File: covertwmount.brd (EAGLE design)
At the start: 50.8 x 33.5 mm, 56 parts, among them J1 B2B-PH-K-S(LF)(SN), U1 STM32G081RBT6, U2 MMBT4401-7-F

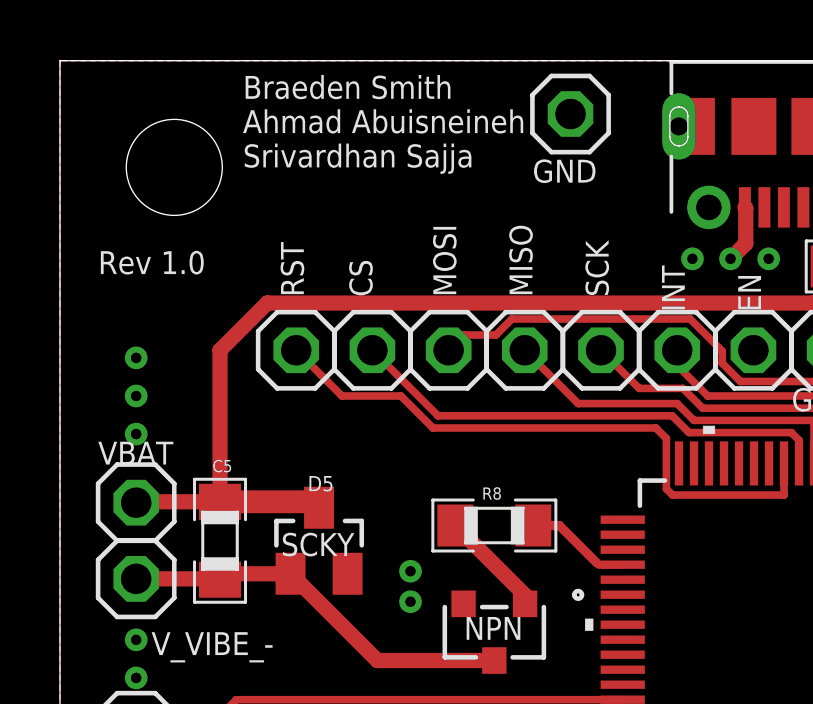
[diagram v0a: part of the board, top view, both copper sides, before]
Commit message: pairing button
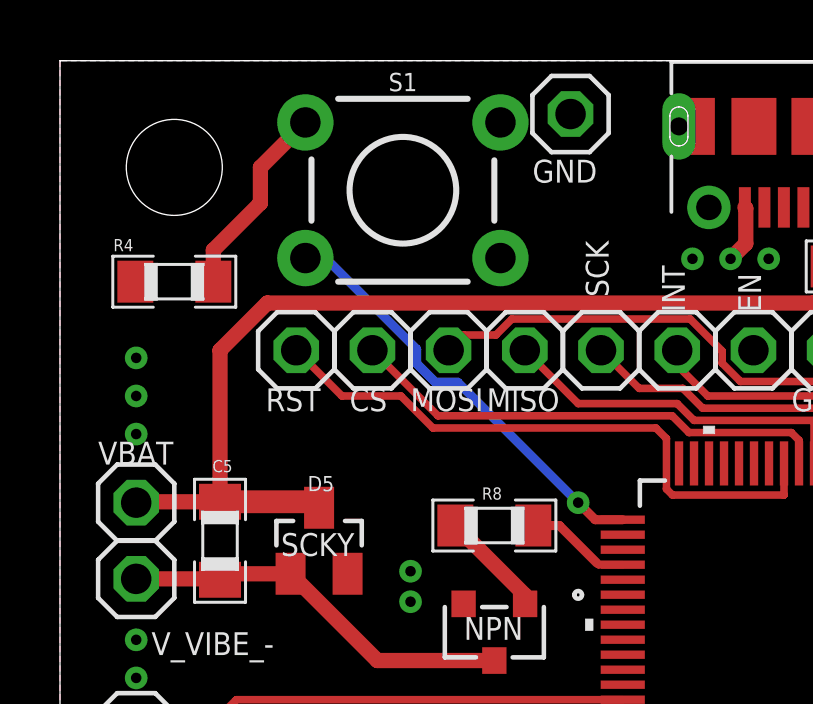
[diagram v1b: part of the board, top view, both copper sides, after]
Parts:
- added R4: 10k, standardparts:0805
- added S1: MOMENTARY-SWITCH-SPST-PTH-6.0MM, SparkFun-Switches:TACTILE_SWITCH_PTH_6.0MM
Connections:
- new net N$9: R4.2, S1.1
- new net PAIR_INT: S1.3, U1.33
- net GND: now also R4.1
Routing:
- net PAIR_INT: track 0.00 -> 14.5 mm, vias 0 -> 1
- net N$9: track 0.00 -> 6.58 mm
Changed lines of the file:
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@@
 <wire x1="50.8" y1="33.528" x2="0" y2="33.528" width="0" layer="20"/>
 <wire x1="0" y1="33.528" x2="0" y2="0" width="0" layer="20"/>
-<text x="1.27" y="26.416" size="0.762" layer="25">Rev 1.0</text>
-<text x="6.096" y="29.972" size="0.762" layer="25">Braeden Smith
+<text x="1.27" y="26.416" size="0.762" layer="26">Rev 1.0</text>
+<text x="6.096" y="28.702" size="0.762" layer="26">Braeden Smith
 Ahmad Abuisneineh
 Srivardhan Sajja</text>
@@
 <text x="30.988" y="20.828" size="0.762" layer="25">TX</text>
 <text x="32.766" y="15.24" size="0.762" layer="25">RX</text>
-<text x="8.128" y="25.654" size="0.762" layer="25" rot="R90">RST</text>
-<text x="10.414" y="25.654" size="0.762" layer="25" rot="R90">CS</text>
-<text x="13.208" y="25.654" size="0.762" layer="25" rot="R90">MOSI</text>
-<text x="15.748" y="25.654" size="0.762" layer="25" rot="R90">MISO</text>
+<text x="6.858" y="21.844" size="0.762" layer="25">RST</text>
+<text x="9.652" y="21.844" size="0.762" layer="25">CS</text>
+<text x="11.684" y="21.844" size="0.762" layer="25">MOSI</text>
+<text x="14.224" y="21.844" size="0.762" layer="25">MISO</text>
 <text x="18.288" y="25.654" size="0.762" layer="25" rot="R90">SCK</text>
 <text x="20.828" y="25.146" size="0.762" layer="25" rot="R90">INT</text>
@@
 <attribute name="VALUE" x="43.434" y="7.239" size="0.4064" layer="27" font="vector"/>
 </element>
+<element name="S1" library="SparkFun-Switches" library_urn="urn:adsk.eagle:library:535" package="TACTILE_SWITCH_PTH_6.0MM" package3d_urn="urn:adsk.eagle:package:40163/1" value="MOMENTARY-SWITCH-SPST-PTH-6.0MM" x="11.43" y="29.21" smashed="yes">
+<attribute name="NAME" x="11.43" y="32.512" size="0.6096" layer="25" font="vector" ratio="20" align="bottom-center"/>
+<attribute name="PROD_ID" value=" SWCH-08441" x="11.43" y="29.21" size="1.778" layer="27" display="off"/>
+<attribute name="SF_SKU" value="COM-00097" x="11.43" y="29.21" size="1.778" layer="27" display="off"/>
+</element>
+<element name="R4" library="standardparts" package="0805" value="10k" x="3.81" y="26.162" smashed="yes">
+<attribute name="NAME" x="1.778" y="27.178" size="0.4064" layer="25" font="vector"/>
+<attribute name="VALUE" x="1.778" y="24.765" size="0.4064" layer="27" font="vector"/>
+</element>
 </elements>
 <signals>
@@
 <via x="15.748" y="2.794" extent="1-16" drill="0.35"/>
 <via x="16.51" y="3.556" extent="1-16" drill="0.35"/>
+<contactref element="R4" pad="1"/>
 </signal>
 <signal name="SPI_SCK">
@@
 <wire x1="24.134" y1="6.346" x2="24.384" y2="6.096" width="0.3048" layer="1"/>
 </signal>
+<signal name="PAIR_INT">
+<contactref element="U1" pad="33"/>
+<contactref element="S1" pad="3"/>
+<via x="17.272" y="18.796" extent="1-16" drill="0.35"/>
+<wire x1="18.7579" y1="18.228" x2="17.84" y2="18.228" width="0.3048" layer="1"/>
+<wire x1="17.84" y1="18.228" x2="17.272" y2="18.796" width="0.3048" layer="1"/>
+<wire x1="17.272" y1="18.796" x2="13.2588" y2="22.8092" width="0.3048" layer="16"/>
+<wire x1="13.2588" y1="22.8092" x2="12.5121125" y2="22.8092" width="0.3048" layer="16"/>
+<wire x1="12.5121125" y1="22.8092" x2="11.8872" y2="23.4341125" width="0.3048" layer="16"/>
+<wire x1="11.8872" y1="23.4341125" x2="11.8872" y2="23.9114875" width="0.3048" layer="16"/>
+<wire x1="11.8872" y1="23.9114875" x2="8.8492875" y2="26.9494" width="0.3048" layer="16"/>
+<wire x1="8.8492875" y1="26.9494" x2="8.1788" y2="26.9494" width="0.3048" layer="16"/>
+</signal>
+<signal name="N$9">
+<contactref element="S1" pad="1"/>
+<contactref element="R4" pad="2"/>
+<wire x1="8.1788" y1="31.4706" x2="6.68" y2="29.9718" width="0.508" layer="1"/>
+<wire x1="6.68" y1="29.9718" x2="6.68" y2="28.78320625" width="0.508" layer="1"/>
+<wire x1="6.68" y1="28.78320625" x2="5.11" y2="27.21320625" width="0.508" layer="1"/>
+<wire x1="5.11" y1="27.21320625" x2="5.11" y2="26.162" width="0.508" layer="1"/>
+</signal>
 </signals>
